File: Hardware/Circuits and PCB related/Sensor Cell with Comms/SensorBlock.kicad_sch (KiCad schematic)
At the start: 15 parts, among them U10 FM24V05, U11 INA3221, U7 TMP75B, U8 TMP75B, U9 TMP75B

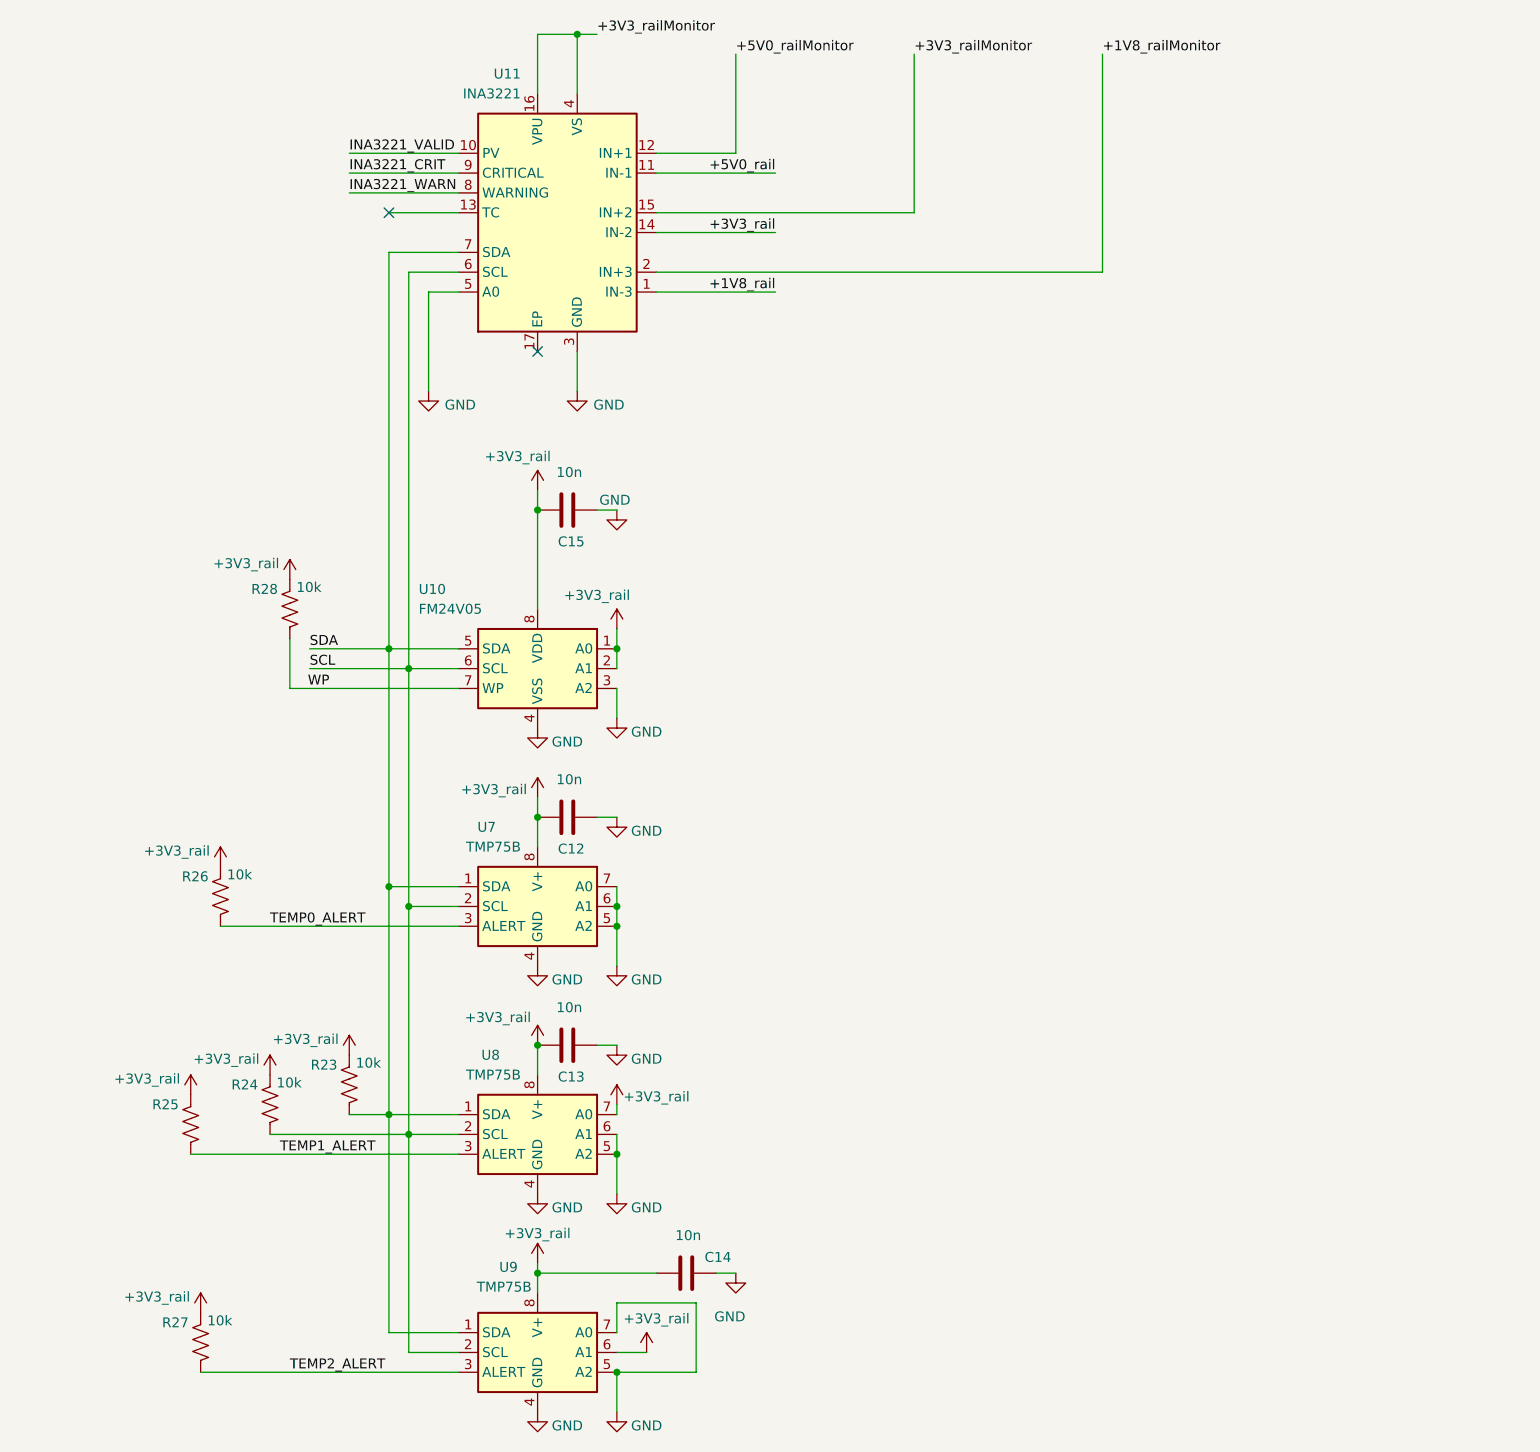
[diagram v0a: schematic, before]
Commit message: Finished schematic, added all footprints, finishing ERC now to move onto the PCB planner to have Kicad do most of the heavy lifting
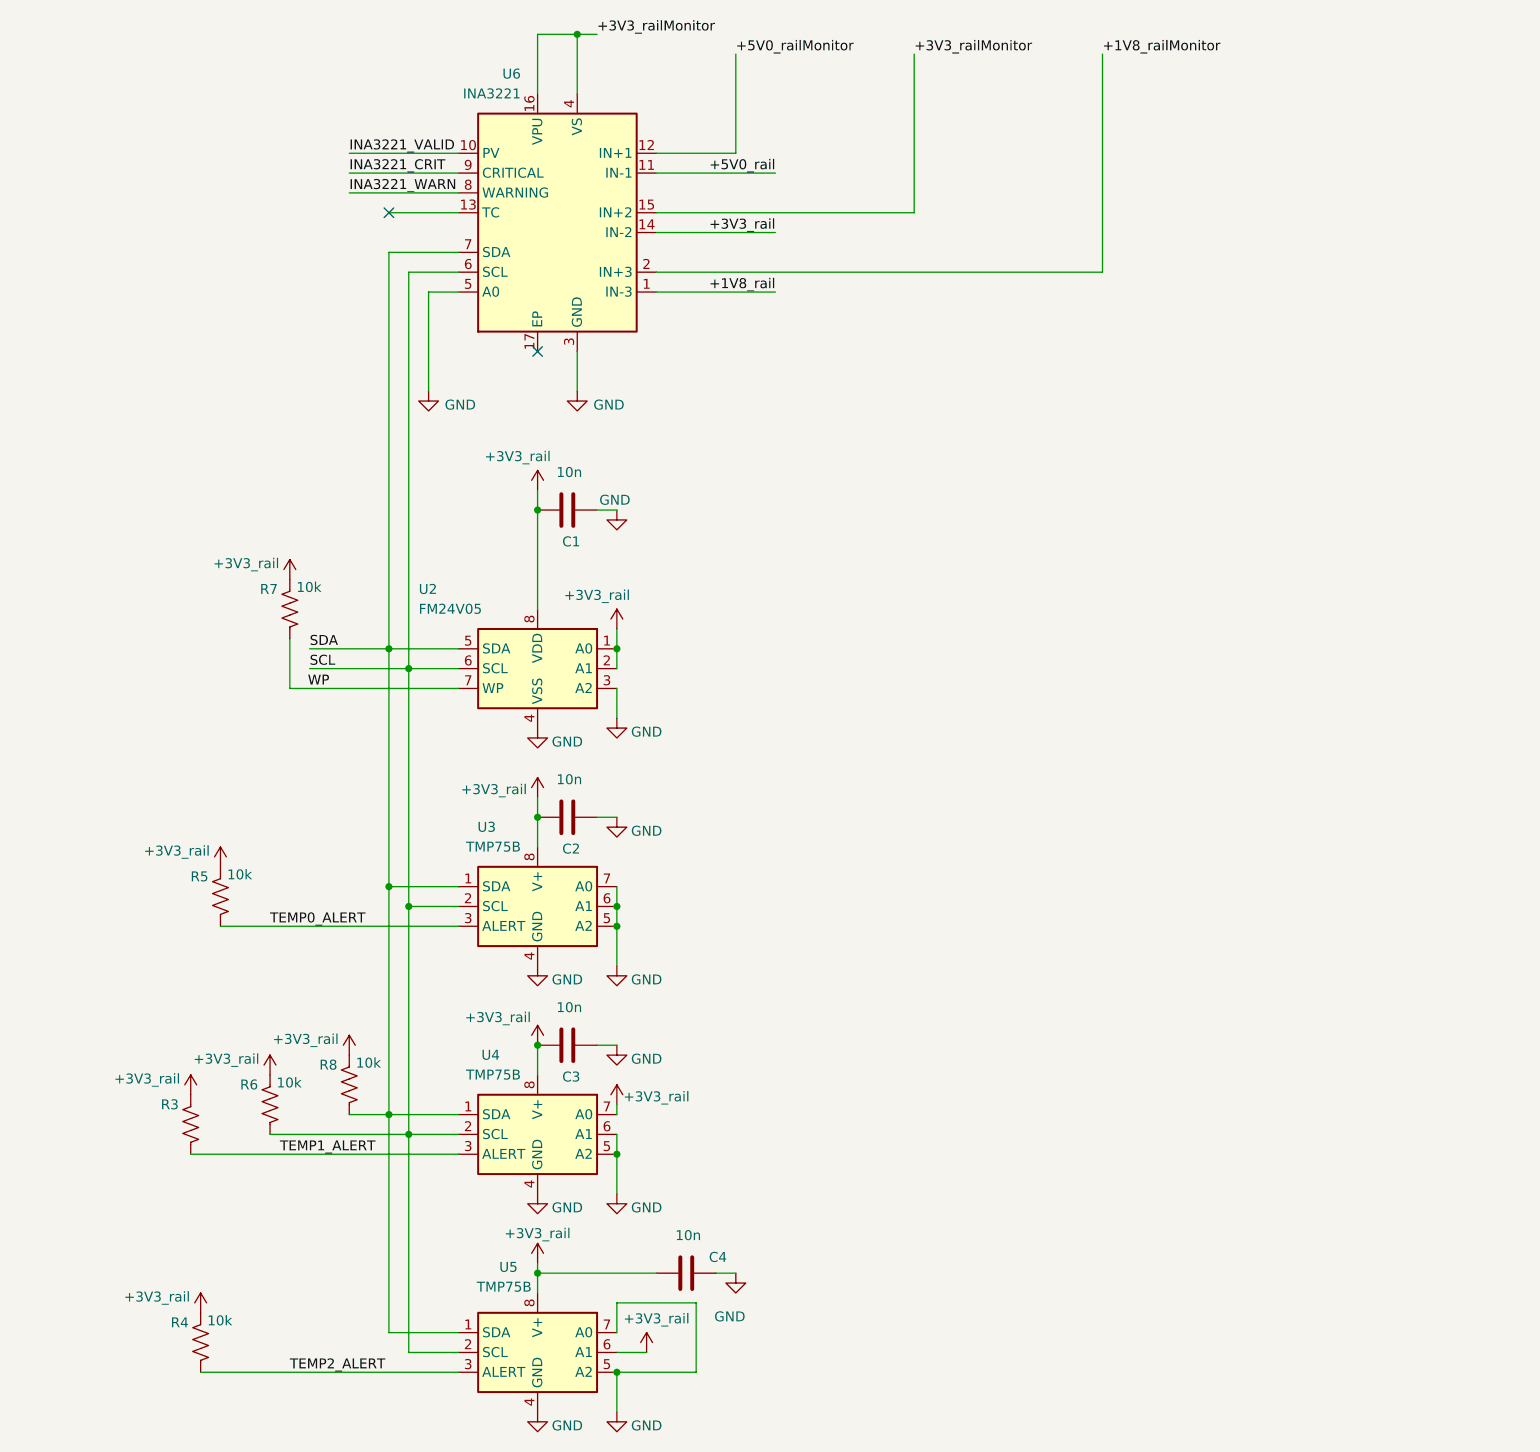
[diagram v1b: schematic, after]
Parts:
- renumbered C15 to C1, C12 to C2, C13 to C3, C14 to C4, R25 to R3, R27 to R4, R26 to R5, R24 to R6, R28 to R7, R23 to R8, U10 to U2, U7 to U3, U8 to U4, U9 to U5, U11 to U6

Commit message: Bulk done to resolve ERC errors, went from 70 to 25. Need to resolve the remaining errors before generation of the PCB. Decided on Hirose Electric Connectors since theyre low profile and locking
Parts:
- U6: footprint Connector_PinHeader_1.00mm:PinHeader_1x08_P1.00mm_Vertical -> footprintLib:PinHeader_1x08_P1.00mm_Vertical_addedMonitorLines
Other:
- moved on the sheet: R7

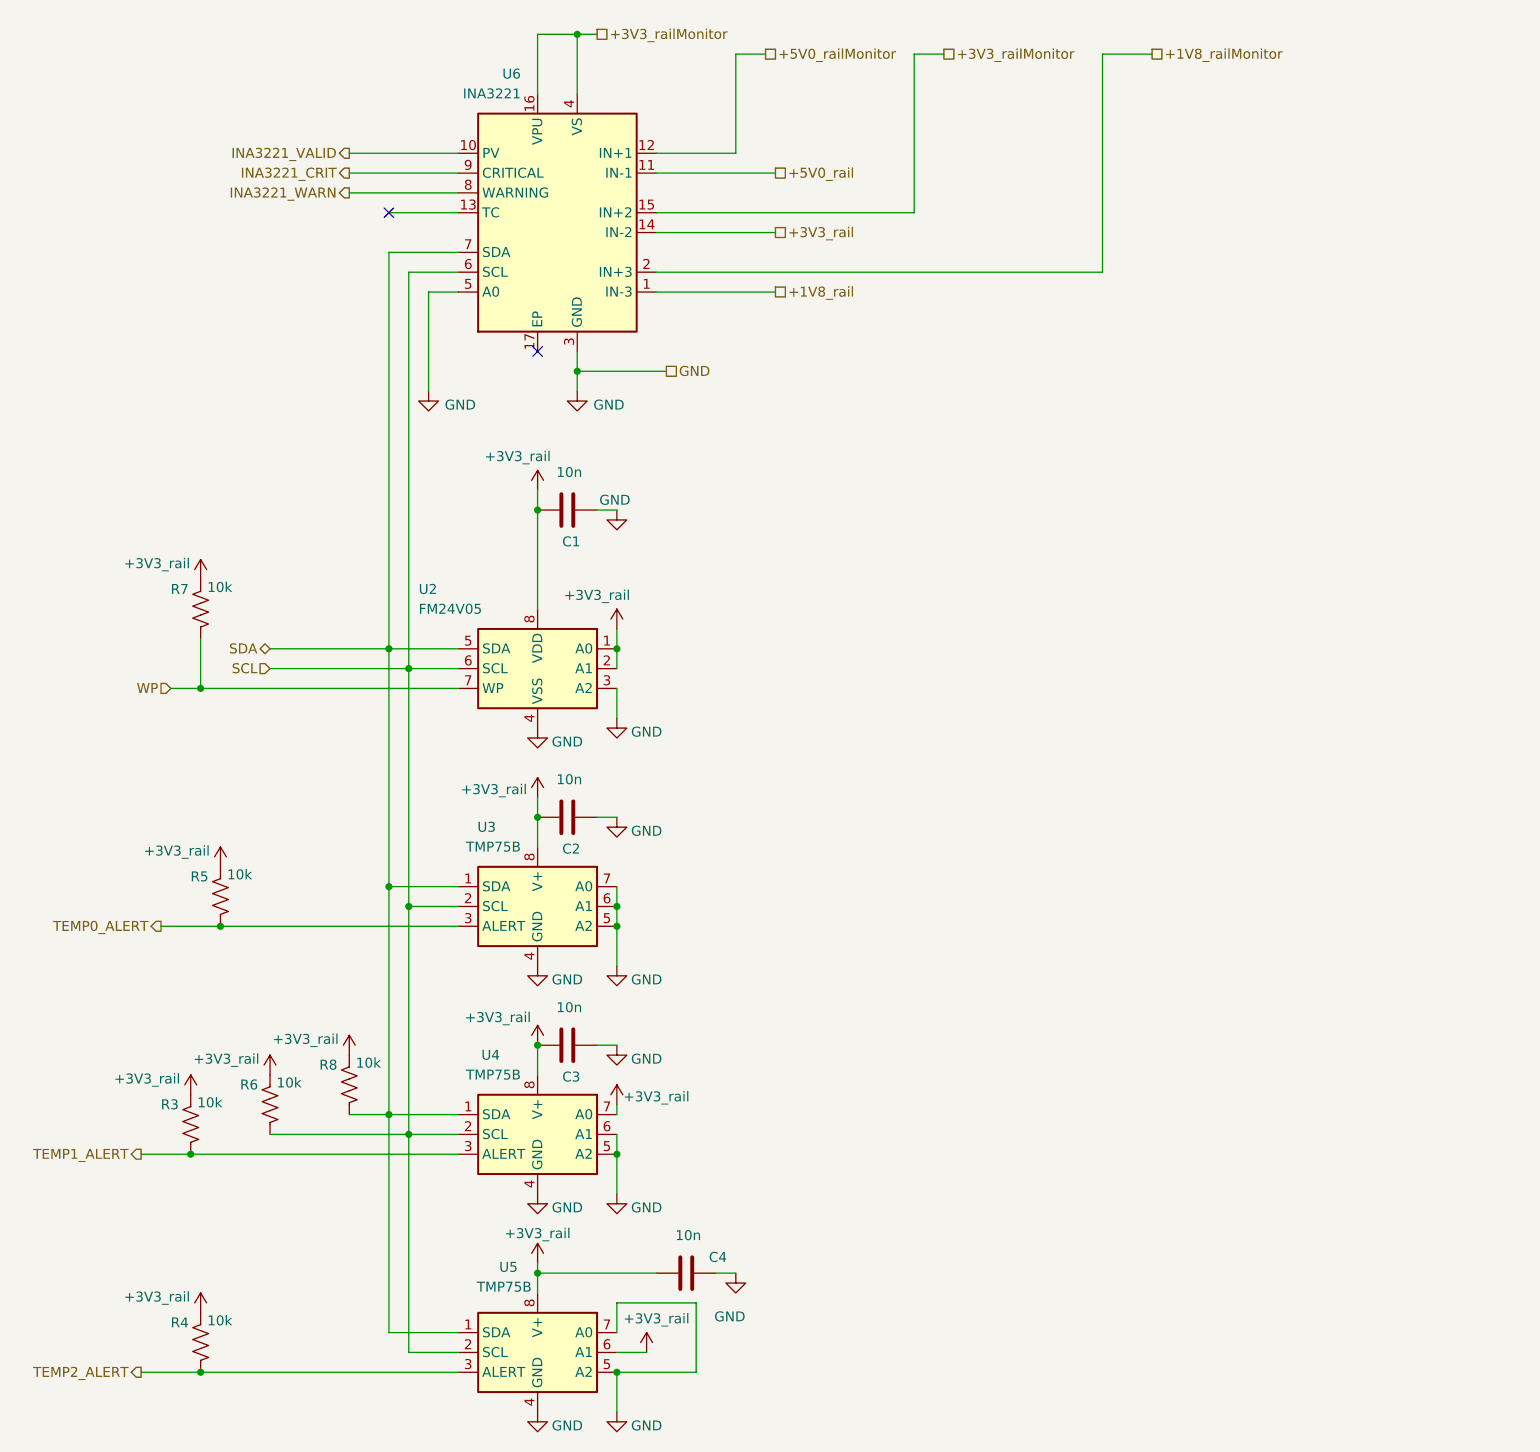
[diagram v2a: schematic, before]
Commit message: Schematic done, and ERC passes successfully. Move onto PCB now that this is completed
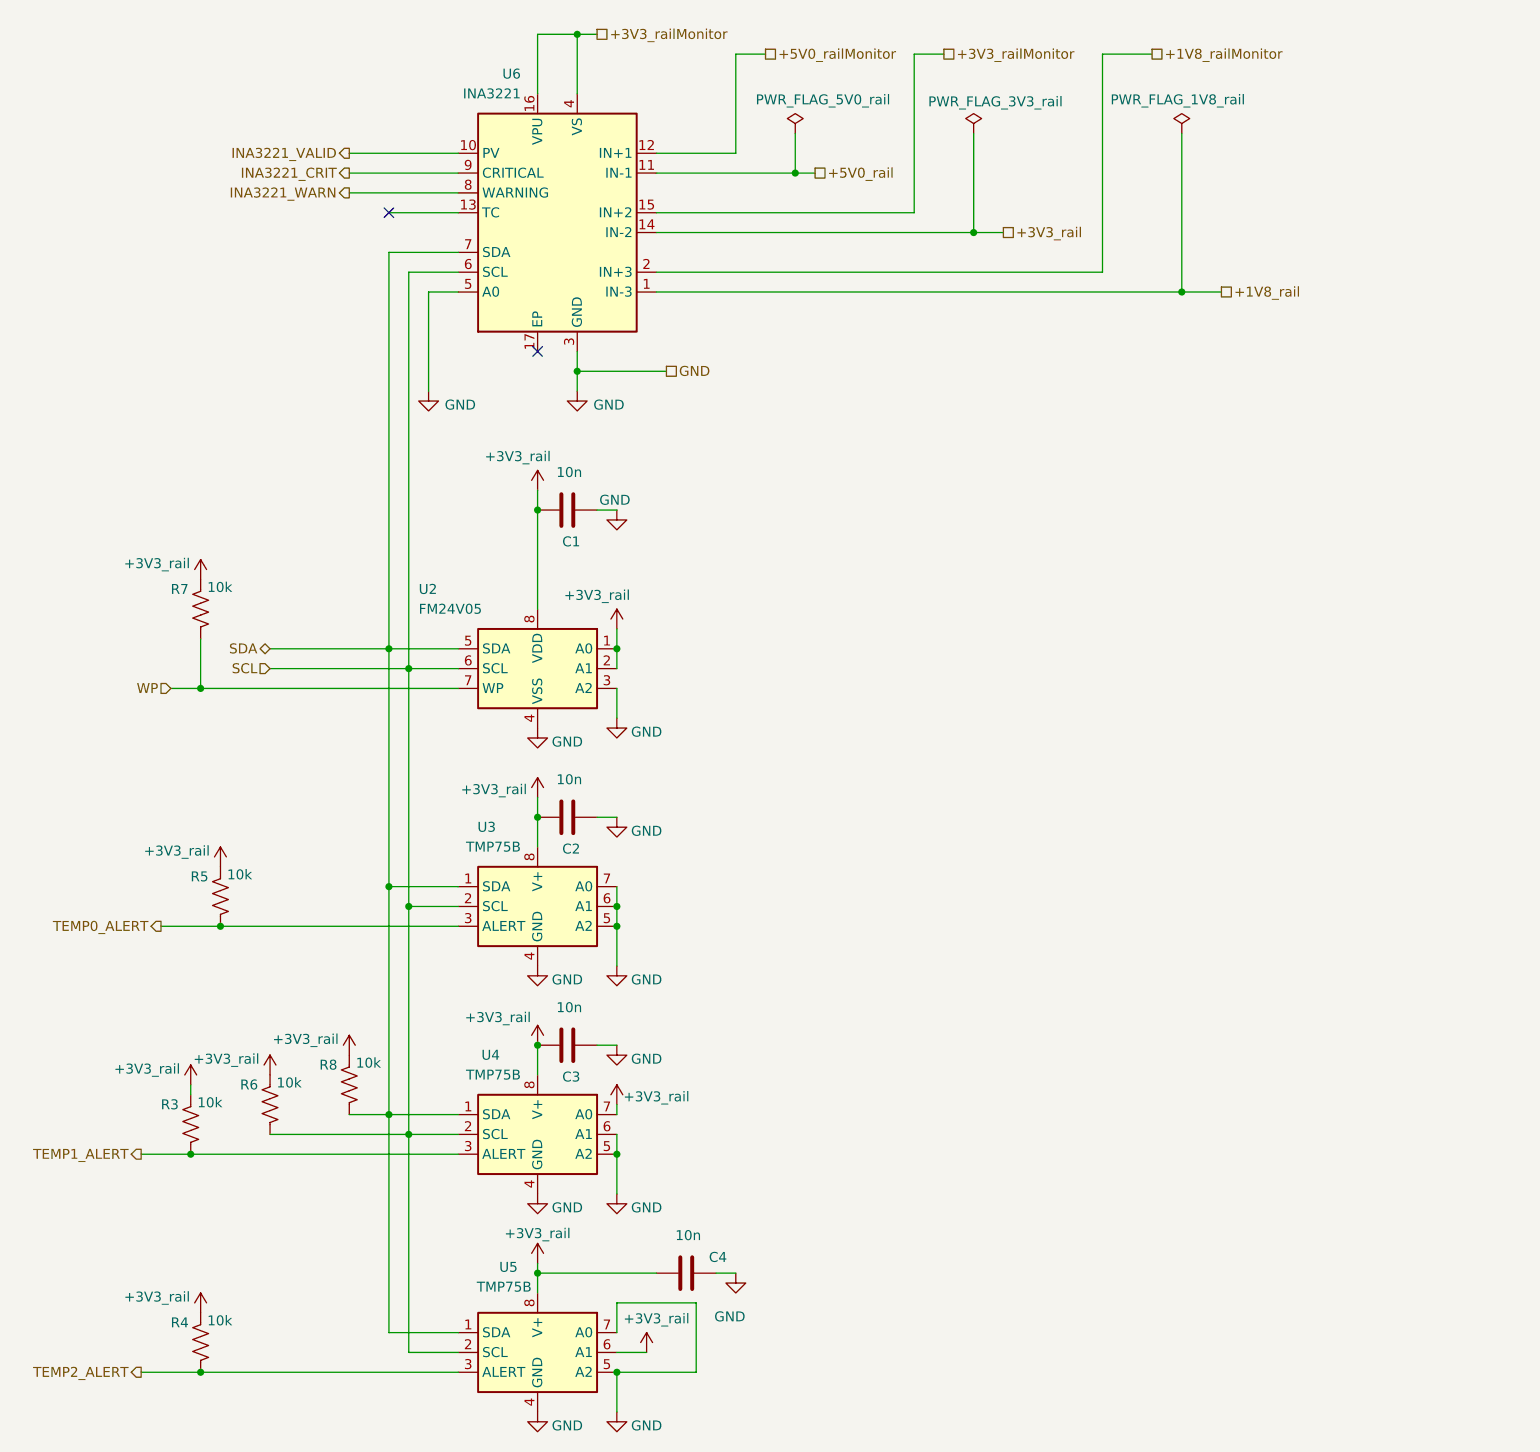
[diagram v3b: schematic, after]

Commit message: First revision of PCB nearly done, Need to finish up 1v8 planes then wire components together
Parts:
- added C24: 10n, Capacitor_SMD:C_0603_1608Metric_Pad1.08x0.95mm_HandSolder, symbol Device:C
- added C25, C26, C27: 10u, Capacitor_SMD:C_0603_1608Metric_Pad1.08x0.95mm_HandSolder, symbol Device:C
- C1, C2, C3, C4: footprint Capacitor_SMD:C_0201_0603Metric_Pad0.64x0.40mm_HandSolder -> Capacitor_SMD:C_0603_1608Metric_Pad1.08x0.95mm_HandSolder
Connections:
- net +1V8_rail: now also C26.2
- net +3V3_rail: now also U6.16 (VPU), U6.4 (VS), C24.2, C25.2
- net +3V3_railMonitor: no longer U6.16 (VPU), U6.4 (VS)
- net +5V0_rail: now also C27.2
- net GND: now also C24.1, C25.1, C26.1, C27.1
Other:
- title: (none) -> IIC related
